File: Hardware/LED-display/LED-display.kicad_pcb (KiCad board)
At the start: 2 copper layers, 137.2 x 127 mm, 118 parts, among them J1 Conn_01x08, U1 74HC595, U2 74HC595, U3 74HC595

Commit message: Updated layout and reduced number of vias
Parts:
- moved G*** 2.62 mm to (203.8, 160.0)
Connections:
- U2 pad 3: Net-(U2-Pad3) -> (no net)
- U2 pad 4: Net-(U2-Pad4) -> (no net)
- U2 pad 5: Net-(U2-Pad5) -> (no net)
- U2 pad 6: Net-(U2-Pad6) -> (no net)
- U2 pad 7: Net-(U2-Pad7) -> (no net)
- U2 pad 9: Net-(U2-Pad9) -> (no net)
- U3 pad 9: Net-(U3-Pad9) -> (no net)
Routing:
- net Net-(D1-Pad2): track 185.4 -> 174.8 mm, vias 14 -> 0
- net Net-(D56-Pad2): track 154.9 -> 145.0 mm, vias 12 -> 0
- net Net-(D78-Pad2): track 165.1 -> 155.2 mm, vias 12 -> 0
- net Net-(D67-Pad2): track 160.0 -> 150.1 mm, vias 12 -> 0
- net /DATA: track 188.0 -> 180.3 mm, vias 8 -> 1
- net Net-(R1-Pad1): track 58.4 -> 51.9 mm, vias 2 -> 0
- net +5V: track 208.9 -> 203.3 mm, vias 4 -> 2
- net Net-(D23-Pad2): track 154.9 -> 150.1 mm, vias 12 -> 0
- net Net-(D34-Pad2): track 149.9 -> 145.0 mm, vias 12 -> 0
- net Net-(D12-Pad2): track 160.0 -> 155.2 mm, vias 12 -> 0
- net Net-(U1-Pad9): track 40.6 -> 36.1 mm
- net Net-(D45-Pad2): track 144.8 -> 140.7 mm, vias 12 -> 0
- net GND: track 228.0 -> 225.3 mm
- net /EOUT: track 198.1 -> 196.3 mm, vias 6 -> 5
- net Net-(R9-Pad1): track 36.8 -> 35.3 mm, vias 2 -> 1
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
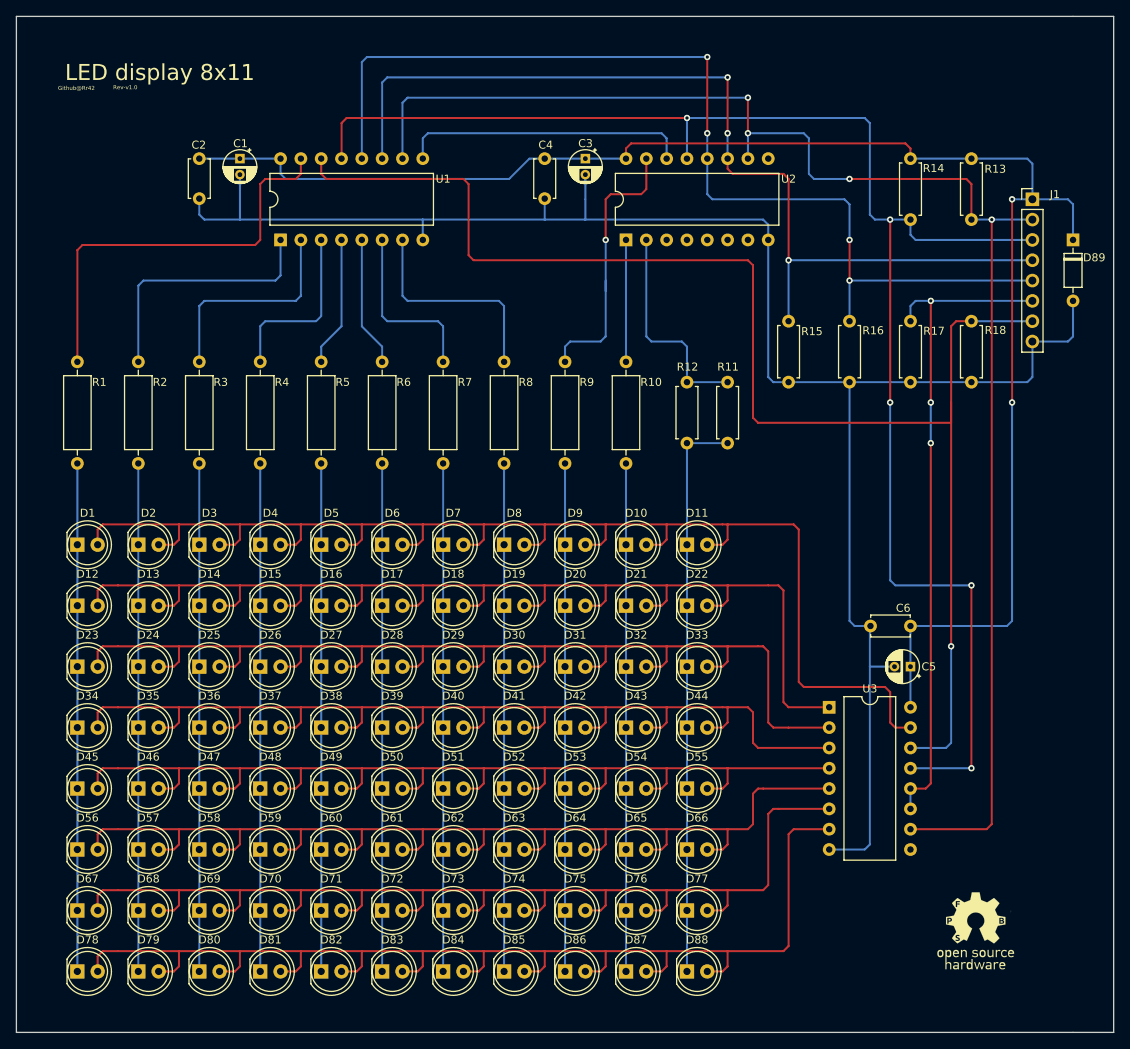
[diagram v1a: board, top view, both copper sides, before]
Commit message: Replaced parllel 2.2K resistors with 1k to match other LEDs
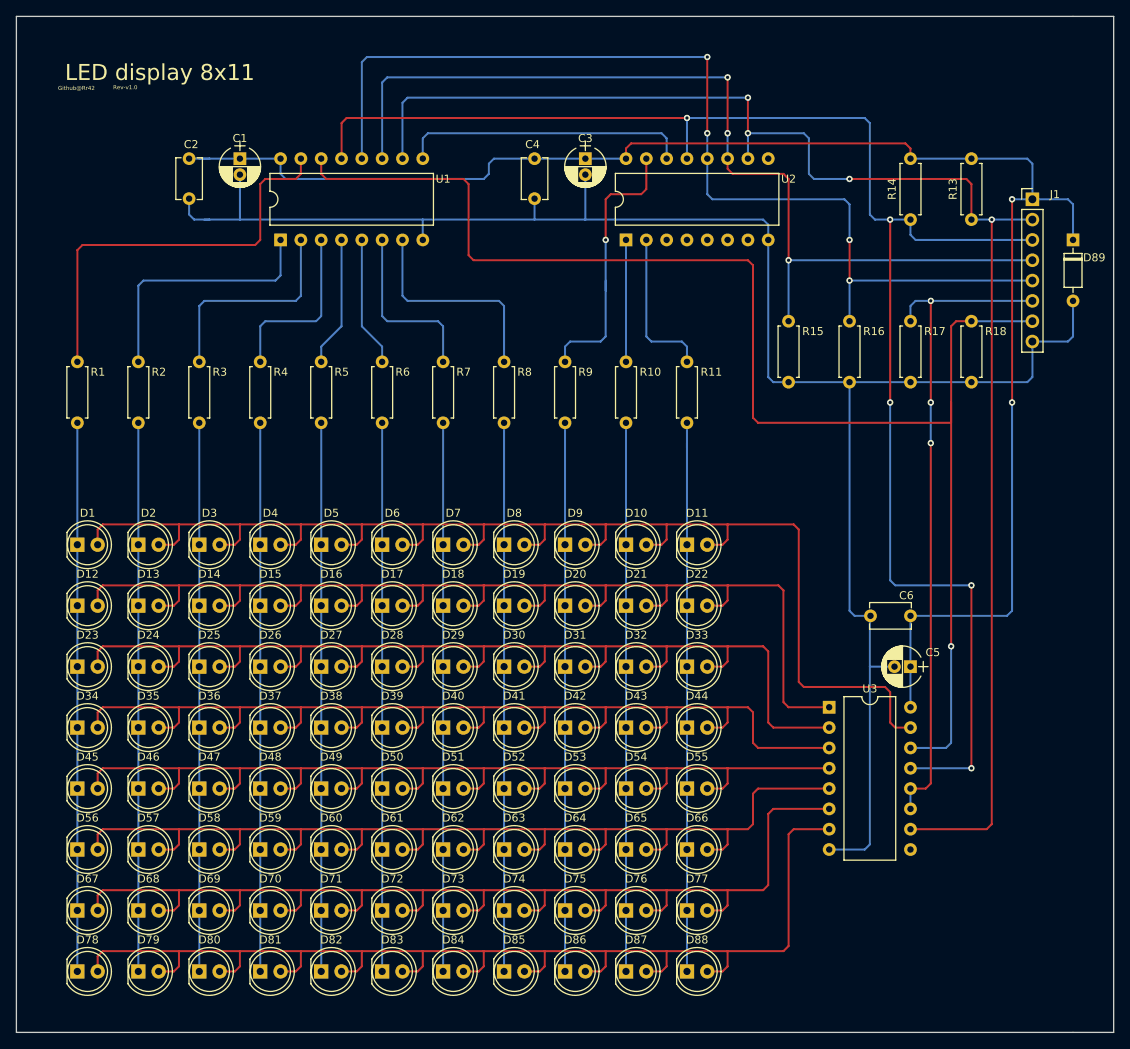
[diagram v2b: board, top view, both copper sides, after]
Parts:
- removed G***: LOGO, LED-display:oshw-spfb
- removed R12: 2.2K, Resistor_THT:R_Axial_DIN0207_L6.3mm_D2.5mm_P7.62mm_Horizontal
- C1, C3, C5: footprint Capacitor_THT:CP_Radial_D4.0mm_P2.00mm -> Capacitors_THT:CP_Radial_D5.0mm_P2.00mm
- C2, C4, C6: footprint Capacitor_THT:C_Disc_D4.7mm_W2.5mm_P5.00mm -> Capacitors_THT:C_Disc_D5.1mm_W3.2mm_P5.00mm
- R1, R10, R2, R3, R4, R5, R6, R7, R8, R9: footprint Resistor_THT:R_Axial_DIN0309_L9.0mm_D3.2mm_P12.70mm_Horizontal -> Resistors_THT:R_Axial_DIN0207_L6.3mm_D2.5mm_P7.62mm_Horizontal
- R11: value 2.2K -> 1K; footprint Resistor_THT:R_Axial_DIN0207_L6.3mm_D2.5mm_P7.62mm_Horizontal -> Resistors_THT:R_Axial_DIN0207_L6.3mm_D2.5mm_P7.62mm_Horizontal
- R13, R14, R15, R16, R17, R18: footprint Resistor_THT:R_Axial_DIN0207_L6.3mm_D2.5mm_P7.62mm_Horizontal -> Resistors_THT:R_Axial_DIN0207_L6.3mm_D2.5mm_P7.62mm_Horizontal
- moved R11 5.68 mm to (167.6, 88.9)
- moved C2 1.27 mm to (105.4, 63.5)
- moved C4 1.27 mm to (148.6, 63.5)
- moved C6 1.27 mm to (195.6, 120.7)
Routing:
- net Net-(R11-Pad1): track 27.2 -> 19.6 mm
- net Net-(D20-Pad1): track 63.5 -> 68.6 mm
- net Net-(D19-Pad1): track 63.5 -> 68.6 mm
- net Net-(D18-Pad1): track 63.5 -> 68.6 mm
- net Net-(D17-Pad1): track 63.5 -> 68.6 mm
- net Net-(D16-Pad1): track 63.5 -> 68.6 mm
- net Net-(D15-Pad1): track 63.5 -> 68.6 mm
- net Net-(D14-Pad1): track 63.5 -> 68.6 mm
- net Net-(D13-Pad1): track 63.5 -> 68.6 mm
- net Net-(D10-Pad1): track 63.5 -> 68.6 mm
- net Net-(D1-Pad1): track 63.5 -> 68.6 mm
- net +5V: track 203.3 -> 206.6 mm
- net Net-(D11-Pad1): track 71.1 -> 69.2 mm
- net GND: track 225.3 -> 227.3 mm

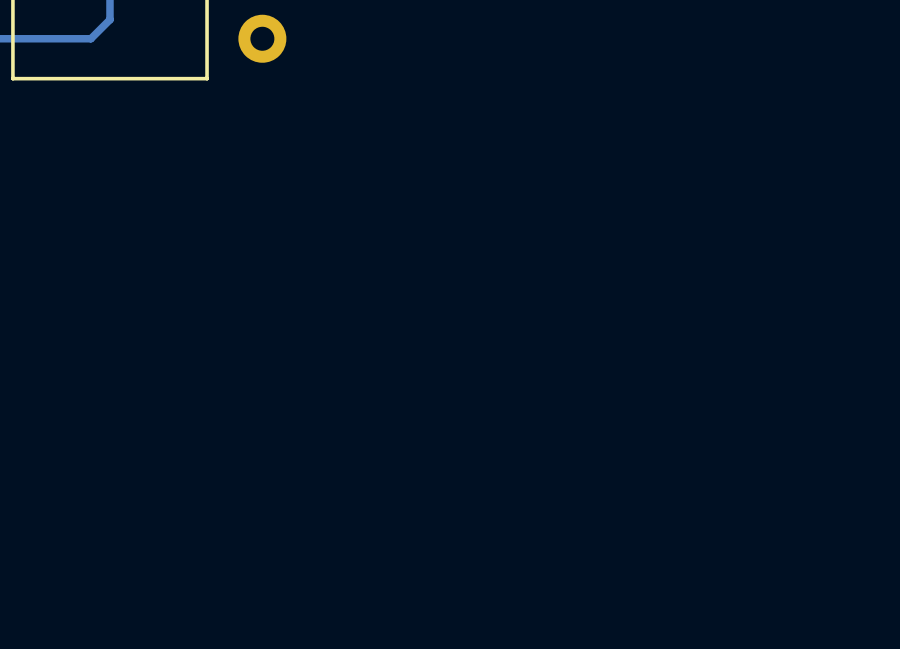
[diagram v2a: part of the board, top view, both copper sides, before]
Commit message: Re-adding oshw logo in layout
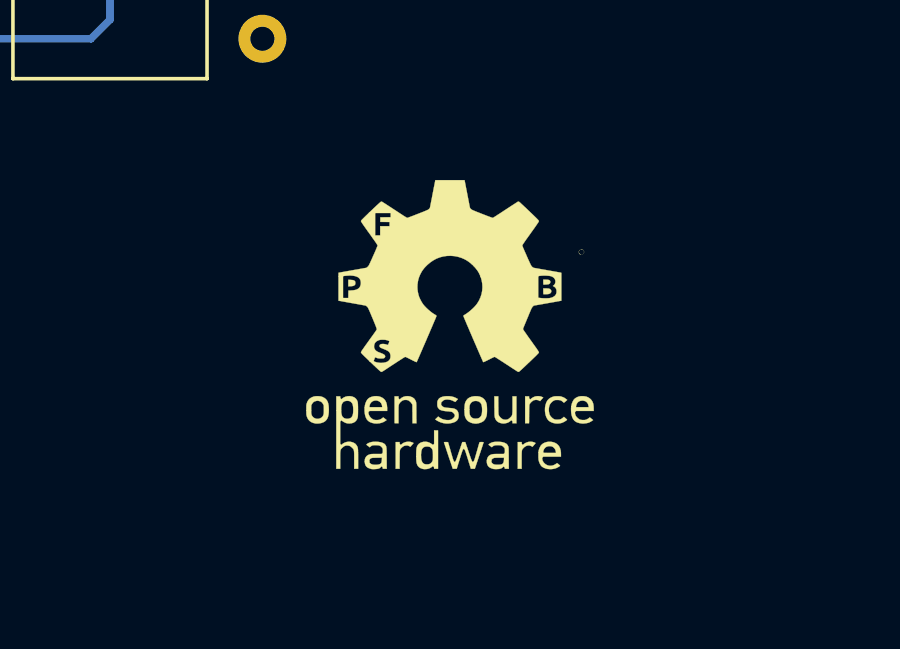
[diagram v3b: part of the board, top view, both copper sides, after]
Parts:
- added G***: LOGO, LED-display:oshw-spfb, F.Cu at (201.9, 159.4)

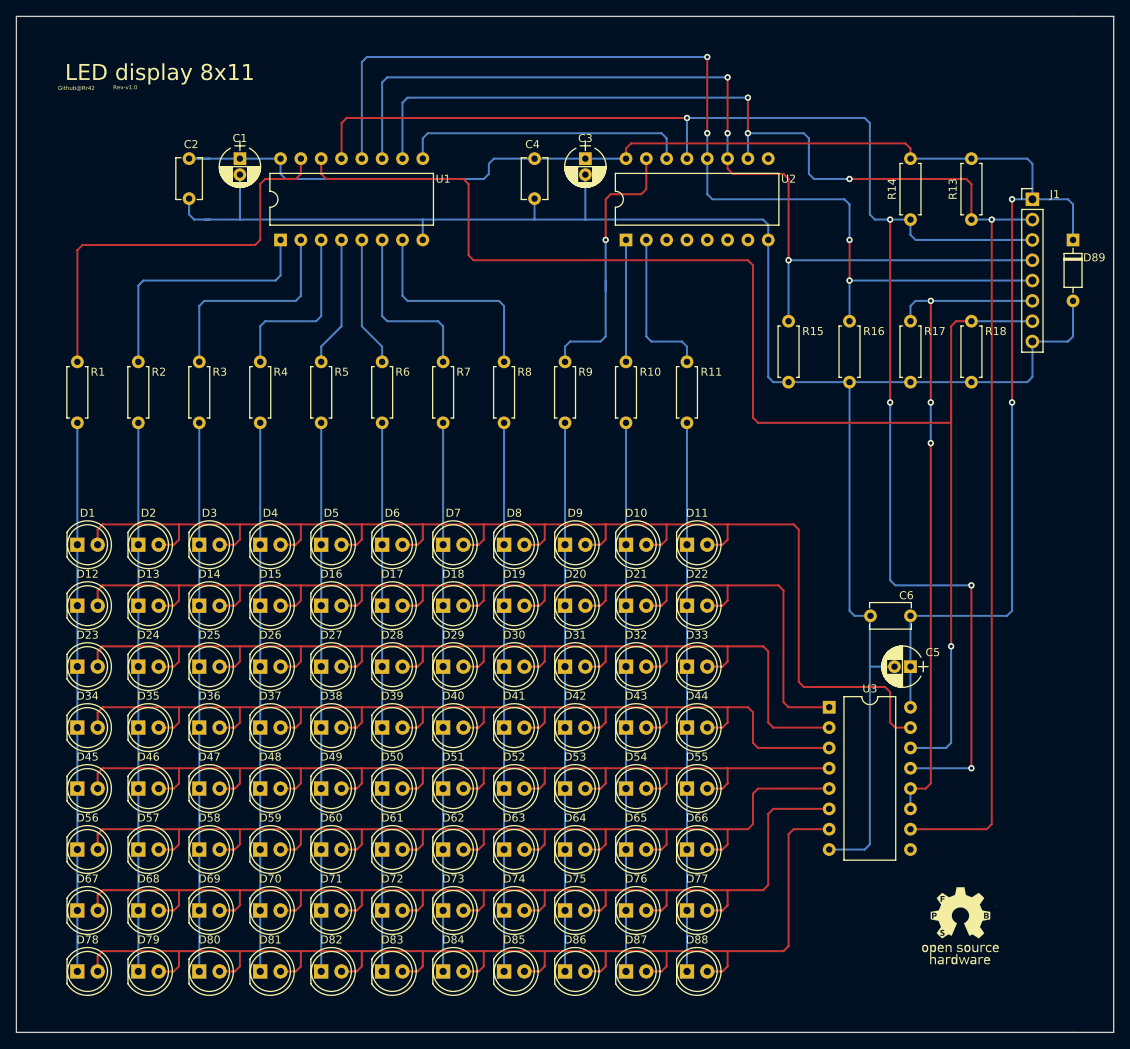
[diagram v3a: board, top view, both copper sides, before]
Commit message: Updating layout with additional headroom for pins > Updating DIP-16 footprint for easier placement > Updating resistor footprints to allow earier placement > Adding silk for connector pin names
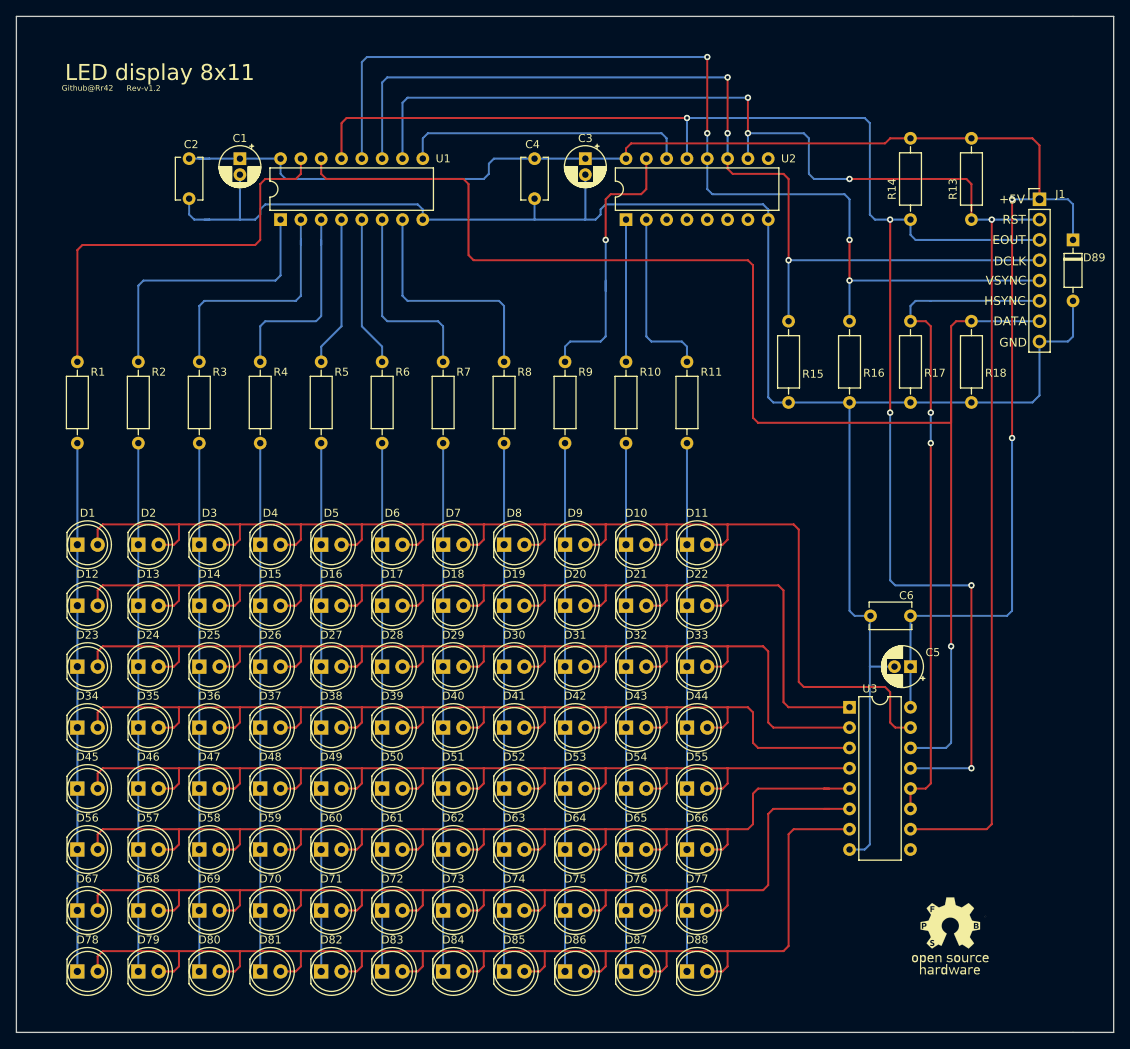
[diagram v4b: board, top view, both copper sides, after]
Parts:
- C1, C3, C5: footprint Capacitors_THT:CP_Radial_D5.0mm_P2.00mm -> Capacitor_THT:CP_Radial_D5.0mm_P2.00mm
- C2, C4, C6: footprint Capacitors_THT:C_Disc_D5.1mm_W3.2mm_P5.00mm -> Capacitor_THT:C_Disc_D5.1mm_W3.2mm_P5.00mm
- R1, R10, R11, R13, R14, R15, R16, R17, R18, R2, R3, R4, R5, R6, R7, R8, R9: footprint Resistors_THT:R_Axial_DIN0207_L6.3mm_D2.5mm_P7.62mm_Horizontal -> Resistor_THT:R_Axial_DIN0207_L6.3mm_D2.5mm_P10.16mm_Horizontal
- U1, U2, U3: footprint Package_DIP:DIP-16_W10.16mm -> Package_DIP:DIP-16_W7.62mm
- moved U3 2.54 mm to (188.0, 132.1)
- moved U1 2.54 mm to (116.8, 71.1)
- moved U2 2.54 mm to (160.0, 71.1)
- moved G*** 1.80 mm to (200.7, 160.7)
- moved J1 0.89 mm to (211.7, 68.6)
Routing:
- net Net-(D67-Pad2): track 150.1 -> 153.3 mm
- net Net-(D56-Pad2): track 145.0 -> 148.2 mm
- net Net-(R3-Pad1): track 27.2 -> 30.4 mm
- net Net-(R4-Pad1): track 22.1 -> 25.3 mm
- net GND: track 227.3 -> 230.3 mm
- net Net-(D45-Pad2): track 140.7 -> 143.2 mm
- net Net-(D34-Pad2): track 145.0 -> 147.6 mm
- net Net-(D23-Pad2): track 150.1 -> 152.6 mm
- net Net-(D12-Pad2): track 155.2 -> 157.7 mm
- net Net-(D20-Pad1): track 68.6 -> 66.0 mm
- net Net-(D19-Pad1): track 68.6 -> 66.0 mm
- net Net-(D18-Pad1): track 68.6 -> 66.0 mm
- net Net-(D17-Pad1): track 68.6 -> 66.0 mm
- net Net-(D16-Pad1): track 68.6 -> 66.0 mm
- net Net-(D15-Pad1): track 68.6 -> 66.0 mm
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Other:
- board text added: "+5V"
- board text added: "DATA"
- board text added: "DCLK"
- board text added: "EOUT"
- board text added: "GND"
- board text added: "HSYNC"
- board text added: "RST"
- board text added: "Rev-v1.2"
- board text added: "VSYNC"
- board text removed: "Rev-v1.0"
